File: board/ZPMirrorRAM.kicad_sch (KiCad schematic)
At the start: 13 parts, among them IC1 74LS219, IC2 74LS219, IC3 74LS219, IC4 74LS219, U16 74F32, U23 74LS154, U24 74F138

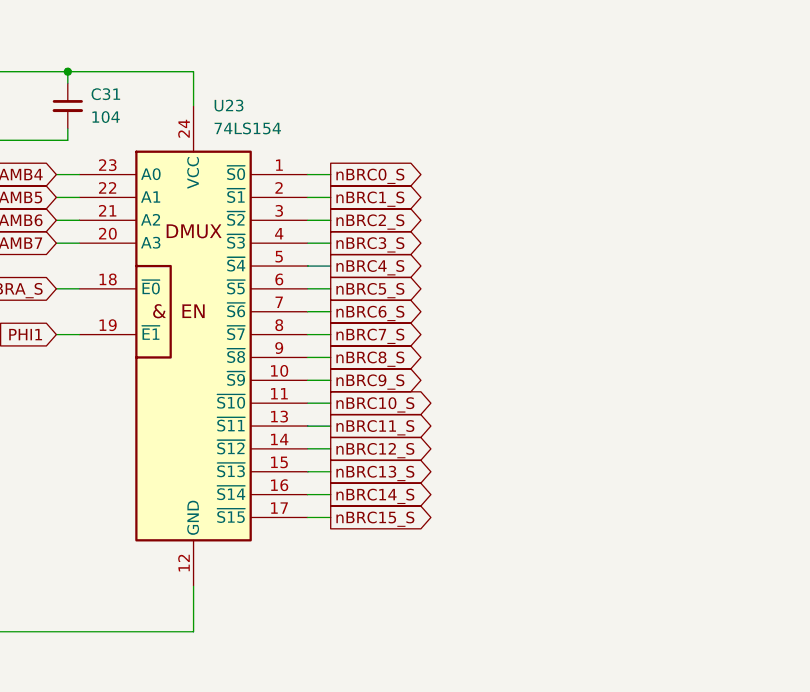
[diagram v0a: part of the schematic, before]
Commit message: V2.0 changes with new S register and simplified logic
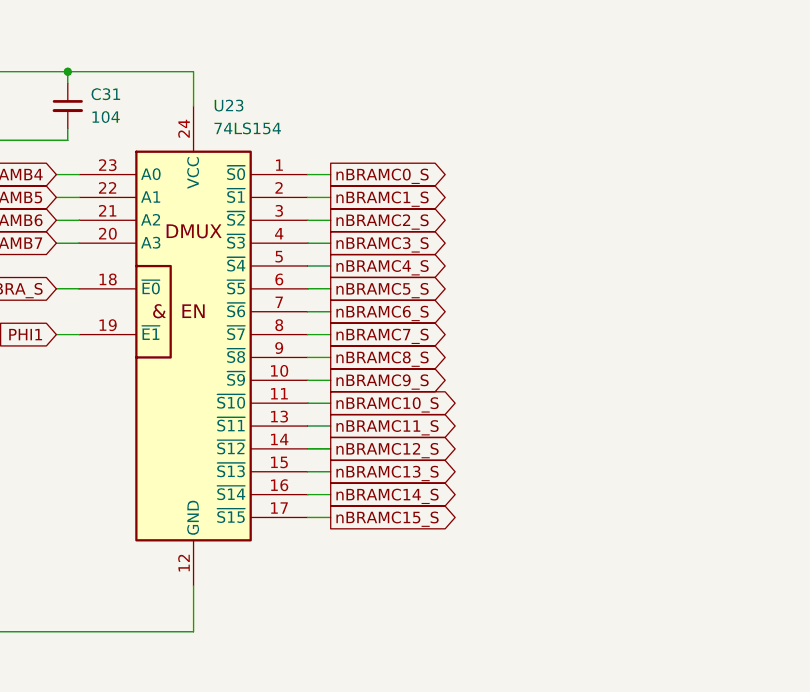
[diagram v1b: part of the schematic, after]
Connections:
- net nBRC0_S renamed nBRAMC0_S
- net nBRC10_S renamed nBRAMC10_S
- net nBRC11_S renamed nBRAMC11_S
- net nBRC12_S renamed nBRAMC12_S
- net nBRC13_S renamed nBRAMC13_S
- net nBRC14_S renamed nBRAMC14_S
- net nBRC15_S renamed nBRAMC15_S
- net nBRC1_S renamed nBRAMC1_S
- net nBRC2_S renamed nBRAMC2_S
- net nBRC3_S renamed nBRAMC3_S
- net nBRC4_S renamed nBRAMC4_S
- net nBRC5_S renamed nBRAMC5_S
- net nBRC6_S renamed nBRAMC6_S
- net nBRC7_S renamed nBRAMC7_S
- net nBRC8_S renamed nBRAMC8_S
- net nBRC9_S renamed nBRAMC9_S
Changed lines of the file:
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@@
 		(title "ZeroPage $00/$01 Mirror Memory and RAM/ROM Bank Logic")
 		(date "2025-10-27")
-		(rev "1.8C")
+		(rev "2.0A")
 		(company "Data Tuning")
 		(comment 1 "Hydra 16")
@@
 		)
 	)
-	(global_label "nBRC1_S"
+	(global_label "nBRAMC1_S"
 		(shape output)
 		(at 195.58 44.45 0)
@@
 		)
 	)
-	(global_label "nBRC2_S"
+	(global_label "nBRAMC2_S"
 		(shape output)
 		(at 195.58 46.99 0)
@@
 		)
 	)
-	(global_label "nBRC15_S"
+	(global_label "nBRAMC15_S"
 		(shape output)
 		(at 195.58 80.01 0)
@@
 		)
 	)
-	(global_label "nBRC7_S"
+	(global_label "nBRAMC7_S"
 		(shape output)
 		(at 195.58 59.69 0)
@@
 		)
 	)
-	(global_label "nBRC8_S"
+	(global_label "nBRAMC8_S"
 		(shape output)
 		(at 195.58 62.23 0)
@@
 		)
 	)
-	(global_label "nBRC14_S"
+	(global_label "nBRAMC14_S"
 		(shape output)
 		(at 195.58 77.47 0)
@@
 		)
 	)
-	(global_label "nBRC12_S"
+	(global_label "nBRAMC12_S"
 		(shape output)
 		(at 195.58 72.39 0)
@@
 		)
 	)
-	(global_label "nBRC4_S"
+	(global_label "nBRAMC4_S"
 		(shape output)
 		(at 195.58 52.07 0)
@@
 		)
 	)
-	(global_label "nBRC11_S"
+	(global_label "nBRAMC11_S"
 		(shape output)
 		(at 195.58 69.85 0)
@@
 		)
 	)
-	(global_label "nBRC6_S"
+	(global_label "nBRAMC6_S"
 		(shape output)
 		(at 195.58 57.15 0)
@@
 		)
 	)
-	(global_label "nBRC9_S"
+	(global_label "nBRAMC9_S"
 		(shape output)
 		(at 195.58 64.77 0)
@@
 		)
 	)
-	(global_label "nBRC5_S"
+	(global_label "nBRAMC5_S"
 		(shape output)
 		(at 195.58 54.61 0)
@@
 		)
 	)
-	(global_label "nBRC3_S"
+	(global_label "nBRAMC3_S"
 		(shape output)
 		(at 195.58 49.53 0)
@@
 		)
 	)
-	(global_label "nBRC10_S"
+	(global_label "nBRAMC10_S"
 		(shape output)
 		(at 195.58 67.31 0)
@@
 		)
 	)
-	(global_label "nBRC0_S"
+	(global_label "nBRAMC0_S"
 		(shape output)
 		(at 195.58 41.91 0)
@@
 		)
 	)
-	(global_label "nBRC13_S"
+	(global_label "nBRAMC13_S"
 		(shape output)
 		(at 195.58 74.93 0)

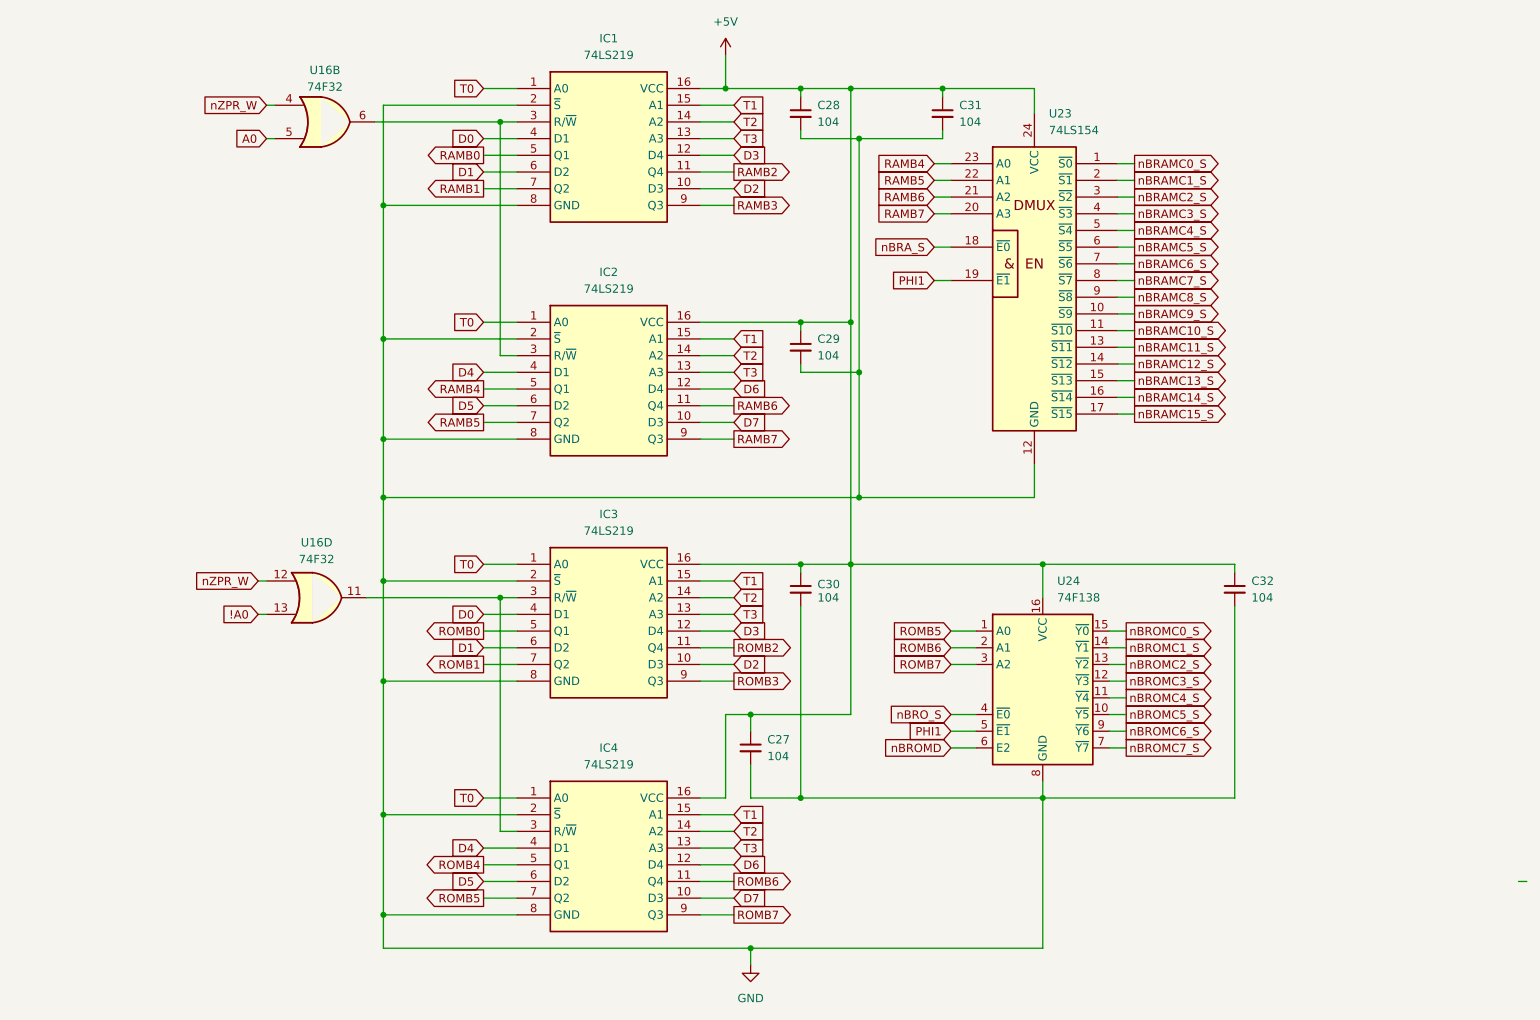
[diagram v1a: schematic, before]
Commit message: V2.0 updates and new hydra breakout and counter cards.
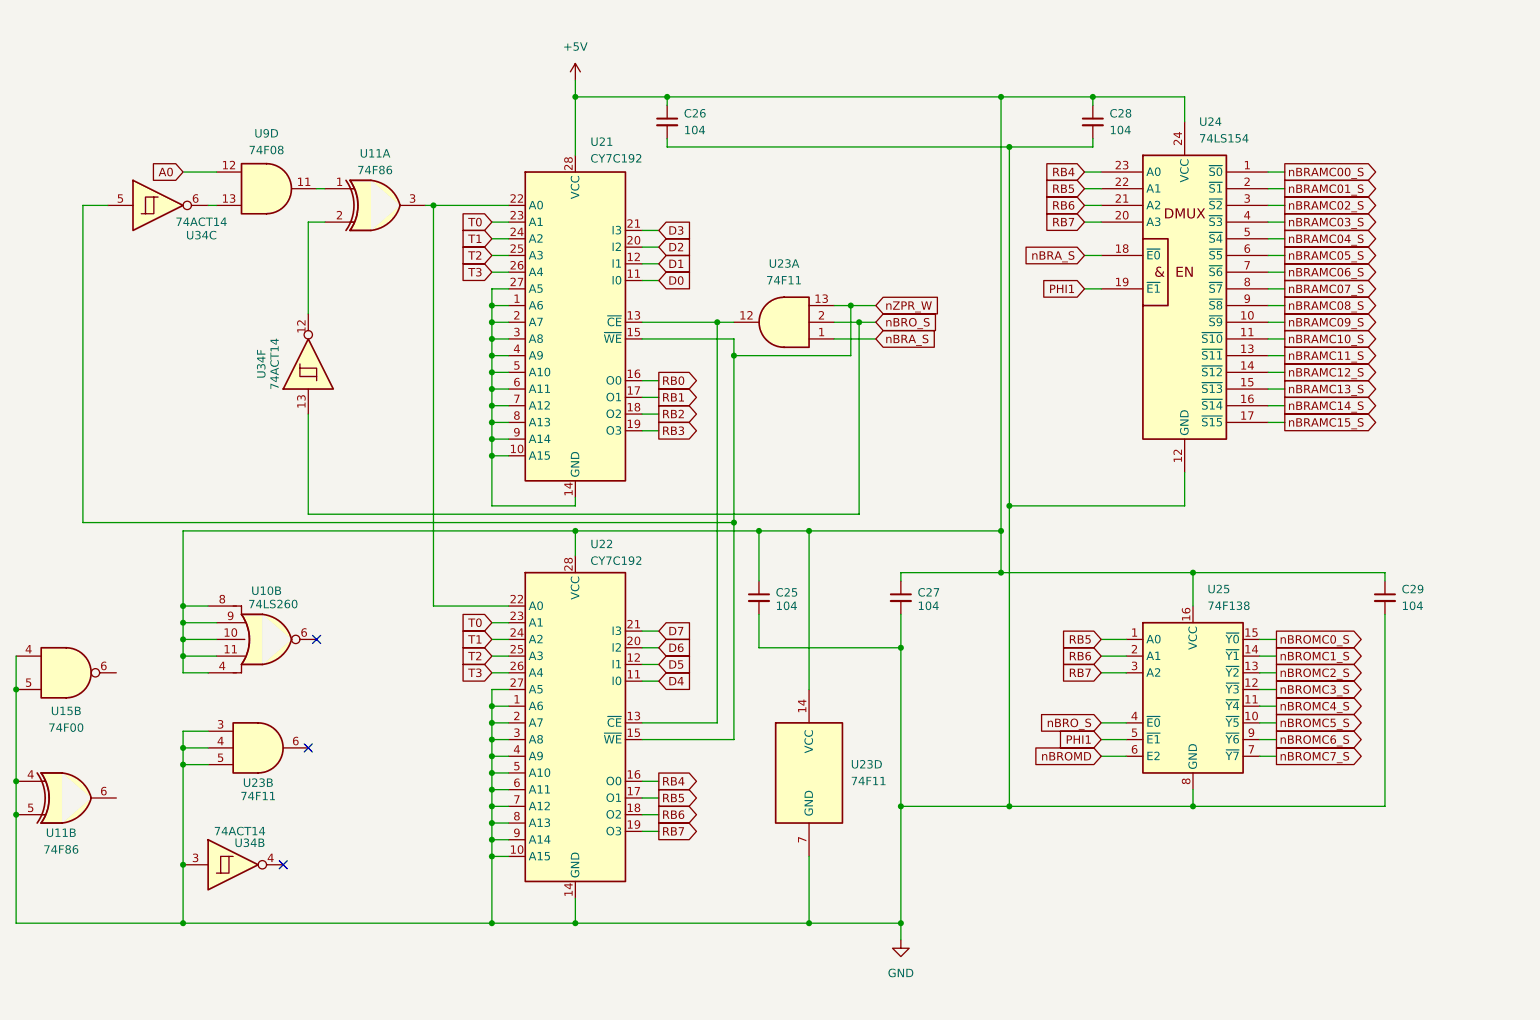
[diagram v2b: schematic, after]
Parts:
- removed C27, C29: 104, Capacitor_THT:C_Disc_D5.0mm_W2.5mm_P5.00mm, symbol Device:C_Small
- removed IC1, IC2, IC3, IC4: 74LS219, Package_DIP:DIP-16_W7.62mm_Socket_LongPads, symbol 74xx:74LS219
- removed U16: 74F32, Package_DIP:DIP-14_W7.62mm_Socket_LongPads, symbol 74xx:74LS32
- added C25: 104, Capacitor_THT:C_Disc_D5.0mm_W2.5mm_P5.00mm, symbol Device:C_Small
- added U10: 74LS260, Package_DIP:DIP-14_W7.62mm_Socket_LongPads, symbol Other_TTL:74LS260
- added U11: 74F86, Package_DIP:DIP-14_W7.62mm_Socket_LongPads, symbol 74xx:74LS86
- added U15: 74F00, Package_DIP:DIP-14_W7.62mm_Socket_LongPads, symbol 74xx:74LS00
- added U21, U22: CY7C192, Package_DIP:DIP-28_W7.62mm_Socket_LongPads, symbol 65XX:6551
- added U23: 74F11, Package_DIP:DIP-14_W7.62mm_Socket_LongPads, symbol 74xx:74LS11
- added U34: 74ACT14, Package_DIP:DIP-14_W7.62mm_Socket_LongPads, symbol 74xx:74HC14
- added U9: 74F08, Package_DIP:DIP-14_W7.62mm_Socket_LongPads, symbol 74xx:74LS08
- renumbered C28 to C26, C30 to C27, C31 to C28, C32 to C29, U23 to U24, U24 to U25
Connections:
- net ROMB5 is gone; now on net RB5: U25.1 (A0)
- net ROMB6 is gone; now on net RB6: U25.2 (A1)
- net ROMB7 is gone; now on net RB7: U25.3 (A2)
- net +5V: now also C25.1, U10.10, U10.11, U10.4, U10.8, U10.9, U21.28 (VCC), U22.28 (VCC), U23.14 (VCC)
- net A0: now also U9.12
- net D0: now also U21.11 (I0)
- net D1: now also U21.12 (I1)
- net D2: now also U21.20 (I2)
- net D3: now also U21.21 (I3)
- net D4: now also U22.11 (I0)
- net D5: now also U22.12 (I1)
- net D6: now also U22.20 (I2)
- net D7: now also U22.21 (I3)
- net GND: now also C25.2, U11.4, U11.5, U15.4, U15.5, U22.1 (A6), U22.10 (A15), U22.14 (GND), U22.2 (A7), U22.27 (A5), U22.3 (A8), U22.4 (A9), U22.5 (A10), U22.6 (A11), U22.7 (A12), U22.8 (A13), U22.9 (A14), U23.3, U23.4, U23.5, U23.7 (GND), U34.3
- net T0: now also U21.23 (A1), U22.23 (A1)
- net T1: now also U21.24 (A2), U22.24 (A2)
- net T2: now also U21.25 (A3), U22.25 (A3)
- net T3: now also U21.26 (A4), U22.26 (A4)
- net nBRA_S: now also U23.1
- net nBRO_S: now also U23.2, U34.13
- net nZPR_W: now also U21.15 (~{WE}), U22.15 (~{WE}), U23.13, U34.5
- net RAMB4 renamed RB4
- net RB4: now also U22.16 (O0)
- net RAMB5 renamed RB5
- net RB5: now also U22.17 (O1)
- net RAMB6 renamed RB6
- net RB6: now also U22.18 (O2)
- net RAMB7 renamed RB7
- net RB7: now also U22.19 (O3)
- net nBRAMC0_S renamed nBRAMC00_S
- net nBRAMC1_S renamed nBRAMC01_S
- net nBRAMC2_S renamed nBRAMC02_S
- net nBRAMC3_S renamed nBRAMC03_S
- net nBRAMC4_S renamed nBRAMC04_S
- net nBRAMC5_S renamed nBRAMC05_S
- net nBRAMC6_S renamed nBRAMC06_S
- net nBRAMC7_S renamed nBRAMC07_S
- net nBRAMC8_S renamed nBRAMC08_S
- net nBRAMC9_S renamed nBRAMC09_S
- new net: U21.13 (~{CE}), U22.13 (~{CE}), U23.12
- new net: U34.6, U9.13
- new net: U21.1 (A6), U21.10 (A15), U21.14 (GND), U21.2 (A7), U21.27 (A5), U21.3 (A8), U21.4 (A9), U21.5 (A10), U21.6 (A11), U21.7 (A12), U21.8 (A13), U21.9 (A14)
- new net: U11.3, U21.22 (A0), U22.22 (A0)
- new net: U11.1, U9.11
- new net: U11.2, U34.12
- new net RB0: U21.16 (O0)
- new net RB1: U21.17 (O1)
- new net RB2: U21.18 (O2)
- new net RB3: U21.19 (O3)
- no-connect marks 0 -> 3
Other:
- moved on the sheet: C26, C27, C28, C29, U24, U25
